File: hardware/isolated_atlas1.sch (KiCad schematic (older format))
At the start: 14 parts, among them J301 CONN_01X02, U301 adm3260, U302 ATLAS_SENSOR

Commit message: Fix SSOP-20 width on the isolator.
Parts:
- U301: footprint SMD_Packages:SSOP-20 -> conservify:SSOP20-53
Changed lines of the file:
@@
 F 0 "U301" H 4400 2750 60  0000 C CNN
 F 1 "adm3260" H 4400 2900 60  0000 C CNN
-F 2 "SMD_Packages:SSOP-20" H 4400 2900 60  0001 C CNN
+F 2 "conservify:SSOP20-53" H 4400 2900 60  0001 C CNN
 F 3 "" H 4400 2900 60  0001 C CNN
 F 4 "584-ADM3260ARSZ" H 0   0   50  0001 C CNN "spn1"

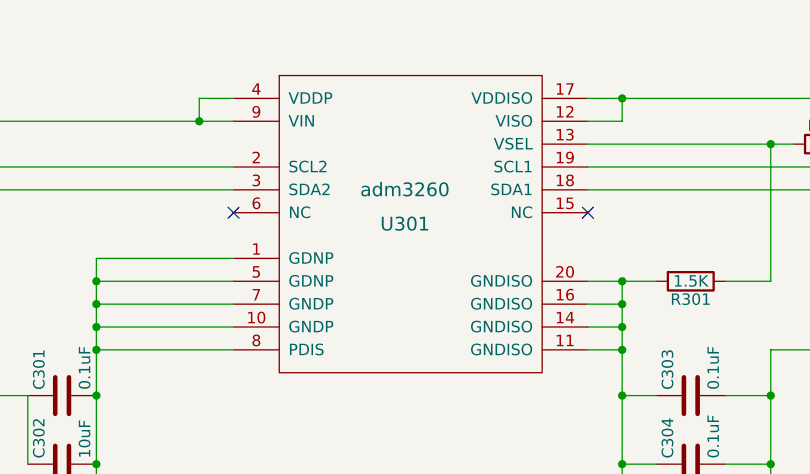
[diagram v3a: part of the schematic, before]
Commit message: Fixing some component names.
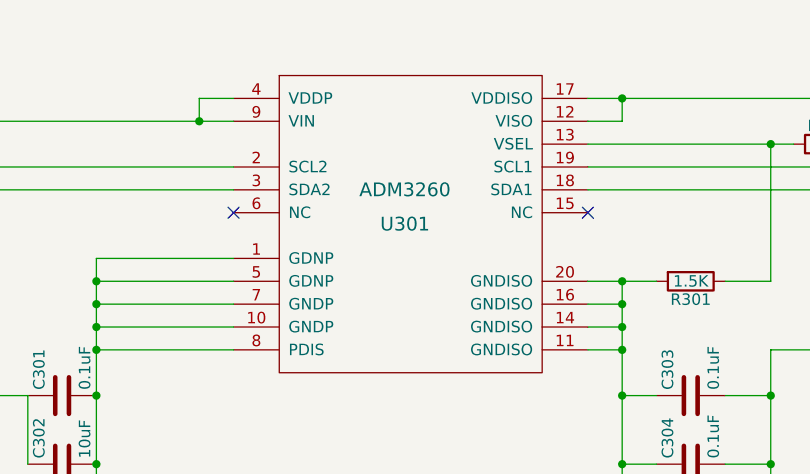
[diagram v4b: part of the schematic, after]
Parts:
- C301, C302, C303, C304, C305, C306, J301, R301, R302, R303, R304, R305, U302: price (none) -> 0
- U301: value adm3260 -> ADM3260; price (none) -> 0

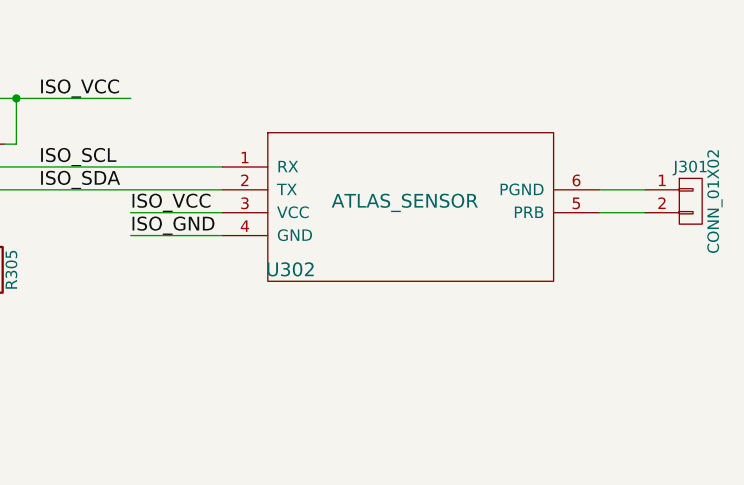
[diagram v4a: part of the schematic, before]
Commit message: Individual atlas sensor values for costing.
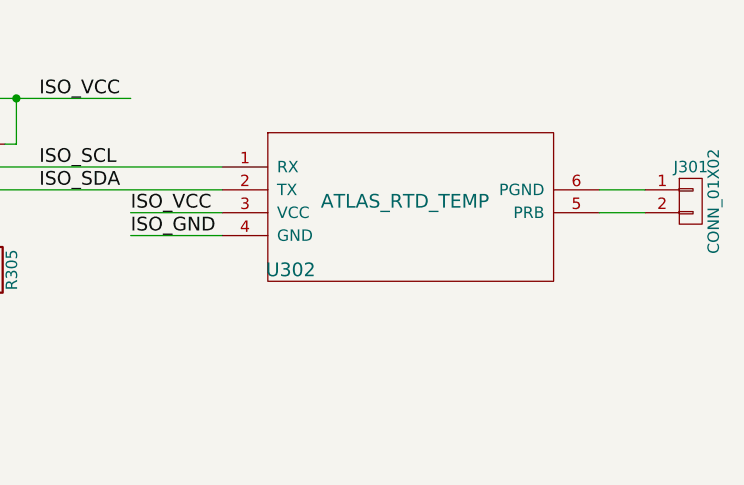
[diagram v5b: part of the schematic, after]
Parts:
- U302: value ATLAS_SENSOR -> ATLAS_RTD_TEMP

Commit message: Normalizing some passive footprints.
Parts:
- C301, C303, C304: footprint Resistors_SMD:R_0603_HandSoldering -> Capacitors_SMD:C_0603_HandSoldering
- C302, C305, C306: footprint Resistors_SMD:R_0603_HandSoldering -> Capacitors_SMD:C_0603_HandSoldering; spn1 810-C1608X7S0J106M -> 81-GRM188R60J106ME47

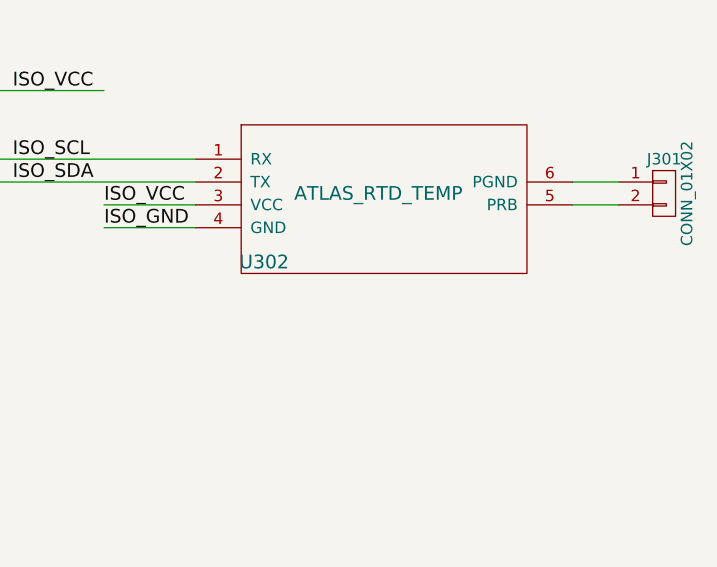
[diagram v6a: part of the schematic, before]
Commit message: Adding placeholders for probes for the BOM.
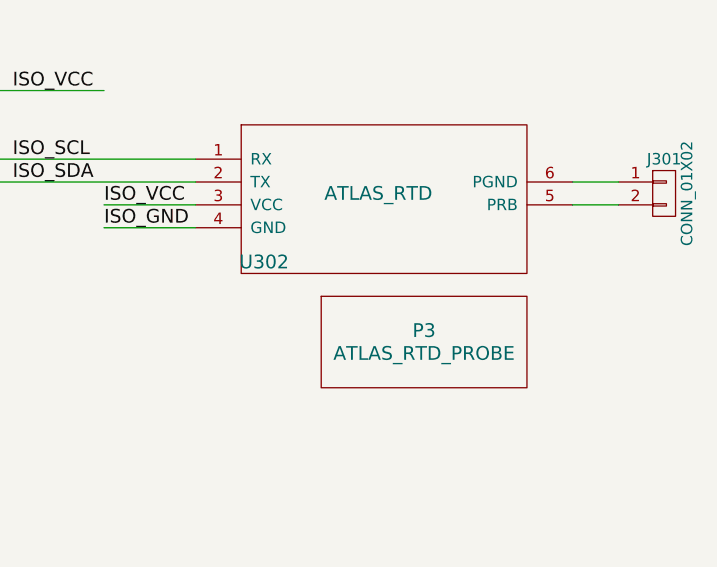
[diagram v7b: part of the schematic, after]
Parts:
- added P3: ATLAS_RTD_PROBE, Oddities:Dummy_Empty, symbol WATER_PROBE
- U302: value ATLAS_RTD_TEMP -> ATLAS_RTD

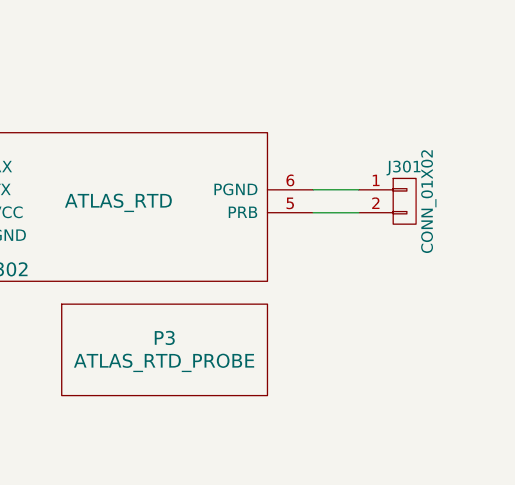
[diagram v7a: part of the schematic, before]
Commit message: Add footprint for OEM Atlas Circuit.
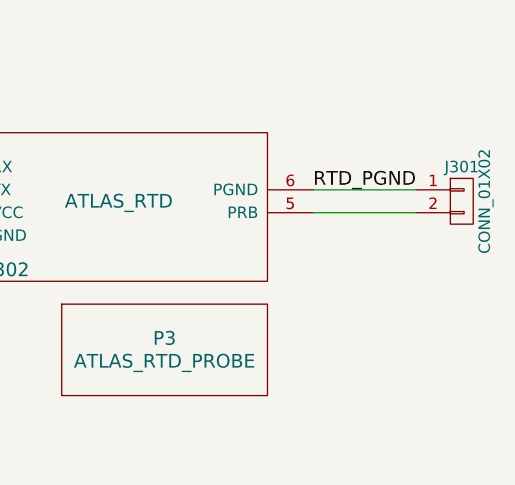
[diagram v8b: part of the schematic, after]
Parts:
- U302: footprint conservify:atlas_sensor_board -> conservify:ATLAS_SENSOR_BOARD_COMBO
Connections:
- net labels added: RTD_PGND
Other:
- moved on the sheet: J301
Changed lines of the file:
@@
 F 0 "U302" H 8100 2550 60  0000 C CNN
 F 1 "ATLAS_RTD" H 8600 2850 60  0000 C CNN
-F 2 "conservify:atlas_sensor_board" H 8550 2900 60  0001 C CNN
+F 2 "conservify:ATLAS_SENSOR_BOARD_COMBO" H 8550 2900 60  0001 C CNN
 F 3 "" H 8550 2900 60  0001 C CNN
 F 4 "0" H 8100 2650 50  0001 C CNN "price"
@@
 L CONN_01X02 J301
 U 1 1 59A1BC7C
-P 9850 2950
-F 0 "J301" H 9850 3100 50  0000 C CNN
-F 1 "CONN_01X02" V 9950 2950 50  0000 C CNN
-F 2 "conservify:BNC" H 9850 2950 50  0001 C CNN
-F 3 "" H 9850 2950 50  0001 C CNN
-F 4 "0" H 9850 3200 50  0001 C CNN "price"
-F 5 "523-31-5431" H 0   0   50  0001 C CNN "spn1"
-	1    9850 2950
+P 10100 2950
+F 0 "J301" H 10100 3100 50  0000 C CNN
+F 1 "CONN_01X02" V 10200 2950 50  0000 C CNN
+F 2 "conservify:BNC" H 10100 2950 50  0001 C CNN
+F 3 "" H 10100 2950 50  0001 C CNN
+F 4 "0" H 10100 3200 50  0001 C CNN "price"
+F 5 "523-31-5431" H 250 0   50  0001 C CNN "spn1"
+	1    10100 2950
 	1    0    0    -1
 $EndComp
@@
 	7400 3000 7800 3000
 Wire Wire Line
-	9450 2900 9650 2900
+	9450 2900 9900 2900
 Wire Wire Line
-	9650 3000 9450 3000
+	9450 3000 9900 3000
 Connection ~ 5350 3500
 Connection ~ 5350 3400
@@
 	1    0    0    -1
 $EndComp
+Text Label 9450 2900 0    60   ~ 0
+RTD_PGND
 $EndSCHEMATC
